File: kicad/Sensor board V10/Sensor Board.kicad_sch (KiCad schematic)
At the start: 48 parts, among them J1 Conn_01x04_Pin, J10 Conn_01x03_Pin, J11 Conn_01x03_Pin, J12 Conn_01x03_Pin, J13 Conn_01x03_Pin, J14 Conn_01x03_Pin, J15 Conn_01x03_Pin, J16 Conn_01x03_Pin, J17 Conn_01x03_Pin, J18 Conn_01x03_Pin, J19 Conn_01x03_Pin, J2 Conn_01x03_Pin, J20 Conn_01x03_Pin, J21 Conn_01x04_Pin, J3 Conn_01x03_Pin, J4 Conn_01x03_Pin, J5 Conn_01x03_Pin, J6 Conn_01x02_Male, J7 Conn_01x04_Pin, J8 Conn_01x03_Pin, J9 Conn_01x03_Pin, U1 LM2596T-5, U2 TJA1051T-3, U3 TXS0108EPW, U4 ESP32-DEVKIT-V1

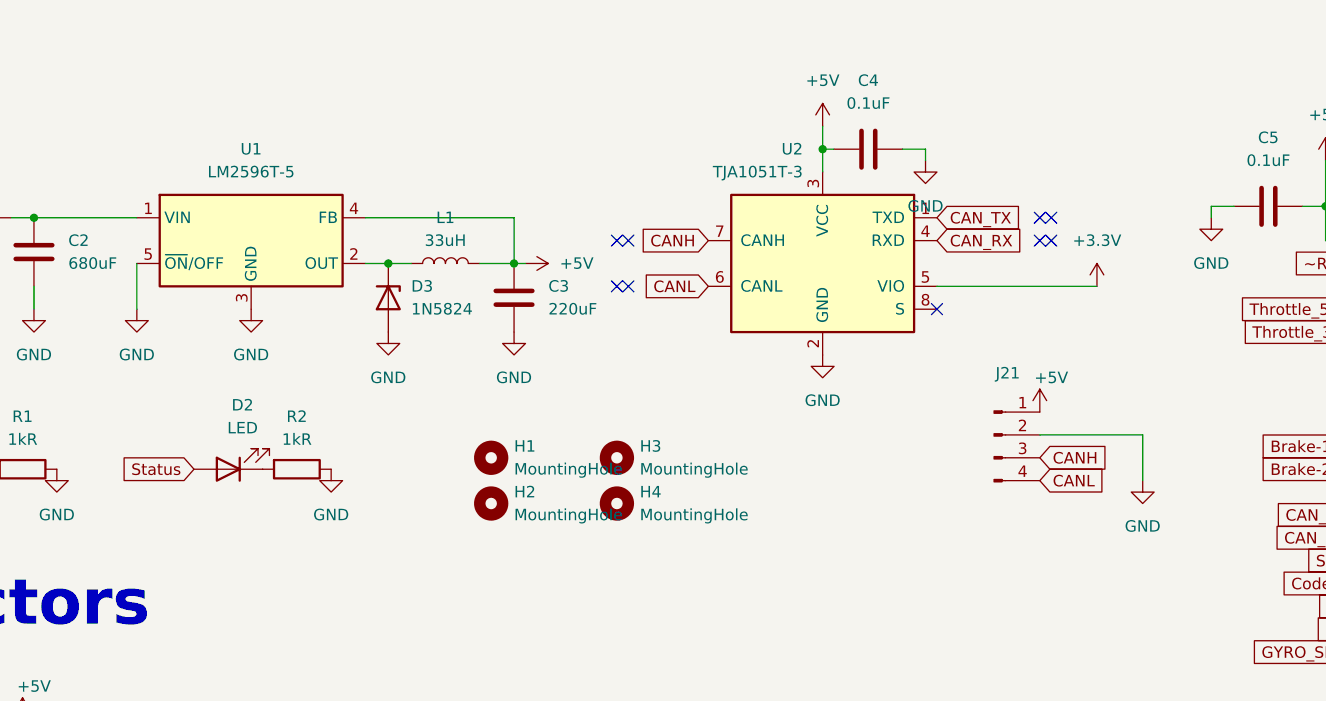
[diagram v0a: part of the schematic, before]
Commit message: Sensor board redesign
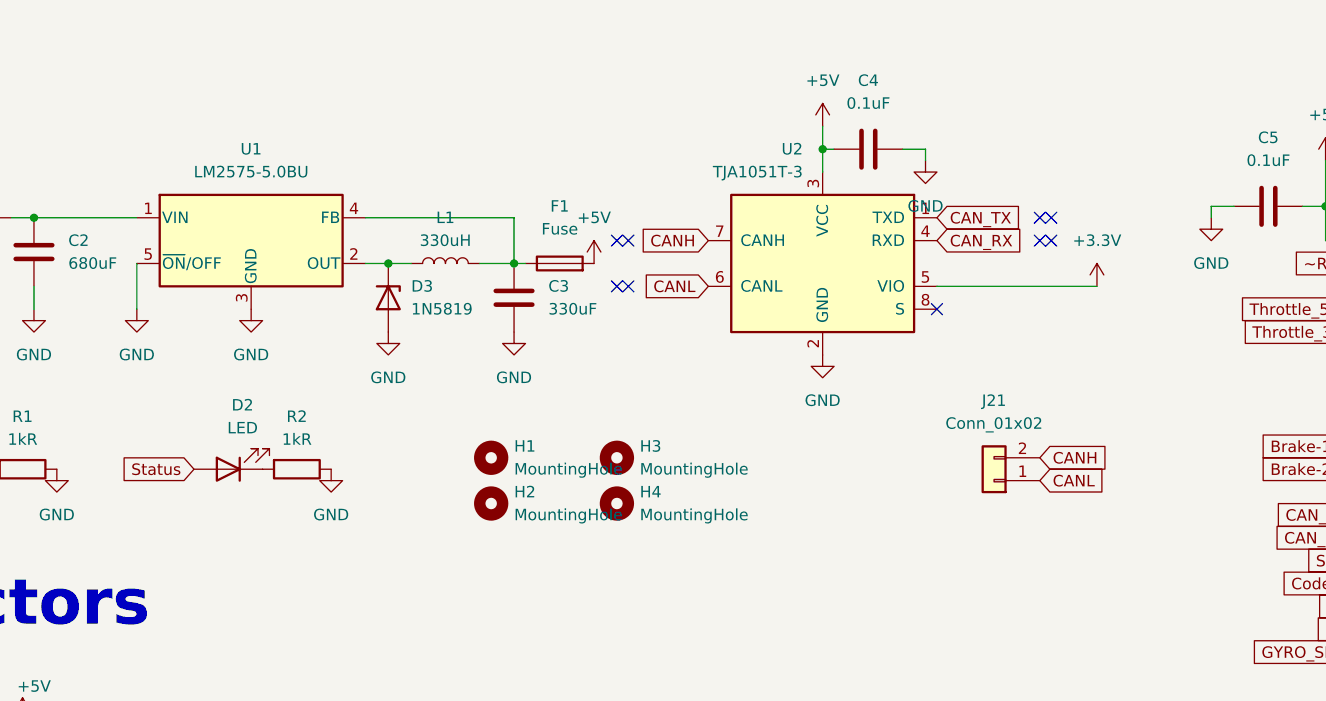
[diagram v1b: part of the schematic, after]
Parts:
- removed J21: Conn_01x04_Pin, Connector_JST:JST_XH_B4B-XH-A_1x04_P2.50mm_Vertical, symbol Connector:Conn_01x04_Pin
- removed U1: LM2596T-5, Package_TO_SOT_THT:TO-220-5_P3.4x3.7mm_StaggerOdd_Lead3.8mm_Vertical, symbol Regulator_Switching:LM2596T-5
- added F1: Fuse, Fuse:Fuse_1210_3225Metric_Pad1.42x2.65mm_HandSolder, symbol Device:Fuse
- added J21: Conn_01x02, Connector_JST:JST_XH_B2B-XH-A_1x02_P2.50mm_Vertical, symbol Connector_Generic:Conn_01x02
- added U1: LM2575-5.0BU, Package_TO_SOT_SMD:TO-263-5_TabPin3, symbol Regulator_Switching:LM2575-5.0BU
- C1, C4, C5, C6, C7: footprint Capacitor_SMD:C_0805_2012Metric_Pad1.18x1.45mm_HandSolder -> RMC_Capacitor:C_0805_2012Metric_Pad1.18x1.45mm_HandSolder_L
- C2: footprint Capacitor_SMD:C_0805_2012Metric_Pad1.18x1.45mm_HandSolder -> RMC_Capacitor:CP_Radial_D10.0mm_P5.00mm_F
- C3: value 220uF -> 330uF; footprint Capacitor_SMD:C_0805_2012Metric_Pad1.18x1.45mm_HandSolder -> RMC_Capacitor:CP_Radial_D10.0mm_P5.00mm_F
- D1, D2: footprint LED_SMD:LED_0805_2012Metric_Pad1.15x1.40mm_HandSolder -> RMC_LED:LED_0805_2012Metric_Pad1.45x1.40mm_HandSolder
- D3: value 1N5824 -> 1N5819
- L1: value 33uH -> 330uH; footprint Inductor_SMD:L_0603_1608Metric_Pad1.05x0.95mm_HandSolder -> RMC_Inductor:L_10.4x10.4_H4.8
- R1, R2, R3, R4, R5, R6, R7, R8: footprint Resistor_SMD:R_0805_2012Metric_Pad1.20x1.40mm_HandSolder -> RMC_Resistor:R_0805_2012Metric_Pad1.20x1.40mm_HandSolder_L
- U3: footprint TXS0108EPW:SOP65P640X120-20N -> Package_SO:TSSOP-20_4.4x6.5mm_P0.65mm
- U4: footprint ESP32-DEVKIT-V1 (1):MODULE_ESP32_DEVKIT_V1 -> ESP32_DEVKIT_V1:MODULE_ESP32_DEVKIT_V1
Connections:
- net +12V: now also U1.1 (VIN)
- net +5V: now also F1.2; no longer C3.1, L1.2
- net CANH: now also J21.2 (Pin_2)
- net CANL: now also J21.1 (Pin_1)
- net GND: now also U1.3 (GND), U1.5 (~{ON}/OFF)
- net at D3.1 (K), L1.1: now also U1.2 (OUT)
- new net: C3.1, F1.1, L1.2, U1.4 (FB)

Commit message: sensor boardvoltage divider
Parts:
- added R10: 2k, symbol Device:R
- added R9: 1k2, symbol Device:R
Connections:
- net +5V: now also R9.1
- net GND: now also R10.2
- new net Signal: R10.1, R9.2
